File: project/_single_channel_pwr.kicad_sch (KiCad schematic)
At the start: 7 parts, among them Q301 AO3400A

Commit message: more layout
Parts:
- renumbered C301 to C13, C302 to C14, C303 to C15, D301 to D7, Q301 to Q2, R301 to R13, R302 to R14
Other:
- title: (none) -> LED Dimmer 6x6
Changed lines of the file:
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@@
 (kicad_sch (version 20211123) (generator eeschema)
   (paper "A4")
+  (title_block
+    (title "LED Dimmer 6x6")
+    (date "2025-01-13")
+    (rev "1.0")
+  )
   (junction (at 125.73 110.49) (diameter 0) (color 0 0 0 0)
   )
@@
   (symbol (lib_id "Transistor_FET:AO3400A") (at 142.24 110.49 0) (unit 1)
     (in_bom yes) (on_board yes)
-    (property "Reference" "Q301" (id 0) (at 144.78 114.3 0)
+    (property "Reference" "Q2" (id 0) (at 144.78 114.3 0)
       (effects (font (size 1.27 1.27)) (justify left))
     )
@@
   (symbol (lib_id "Device:C") (at 151.13 109.22 0) (unit 1)
     (in_bom yes) (on_board yes)
-    (property "Reference" "C303" (id 0) (at 152.4 106.68 0)
+    (property "Reference" "C15" (id 0) (at 152.4 106.68 0)
       (effects (font (size 1.27 1.27)) (justify left))
     )
@@
   (symbol (lib_id "Device:D_Schottky") (at 144.78 101.6 270) (unit 1)
     (in_bom yes) (on_board yes)
-    (property "Reference" "D301" (id 0) (at 138.43 99.06 90)
+    (property "Reference" "D7" (id 0) (at 138.43 99.06 90)
       (effects (font (size 1.27 1.27)) (justify left))
     )
@@
   (symbol (lib_id "Device:C") (at 125.73 114.3 0) (unit 1)
     (in_bom yes) (on_board yes)
-    (property "Reference" "C301" (id 0) (at 127 111.76 0)
+    (property "Reference" "C13" (id 0) (at 127 111.76 0)
       (effects (font (size 1.27 1.27)) (justify left))
     )
@@
   (symbol (lib_id "Device:C") (at 151.13 101.6 0) (unit 1)
     (in_bom yes) (on_board yes)
-    (property "Reference" "C302" (id 0) (at 152.4 99.06 0)
+    (property "Reference" "C14" (id 0) (at 152.4 99.06 0)
       (effects (font (size 1.27 1.27)) (justify left))
     )
@@
   (symbol (lib_id "Device:R") (at 134.62 114.3 180) (unit 1)
     (in_bom yes) (on_board yes)
-    (property "Reference" "R302" (id 0) (at 137.16 111.76 90)
+    (property "Reference" "R14" (id 0) (at 137.16 111.76 90)
       (effects (font (size 1.27 1.27)) (justify left))
     )
@@
   (symbol (lib_id "-pwr:GND") (at 144.78 118.11 0) (unit 1)
     (in_bom yes) (on_board yes)
-    (property "Reference" "#PWR0302" (id 0) (at 144.78 124.46 0)
+    (property "Reference" "#PWR033" (id 0) (at 144.78 124.46 0)
       (effects (font (size 1.27 1.27)) hide)
     )
@@
   (symbol (lib_id "power:+24V") (at 144.78 97.79 0) (unit 1)
     (in_bom yes) (on_board yes)
-    (property "Reference" "#PWR0301" (id 0) (at 144.78 101.6 0)
+    (property "Reference" "#PWR032" (id 0) (at 144.78 101.6 0)
       (effects (font (size 1.27 1.27)) hide)
     )
@@
   (symbol (lib_id "Device:R") (at 120.65 110.49 90) (unit 1)
     (in_bom yes) (on_board yes)
-    (property "Reference" "R301" (id 0) (at 123.19 107.95 90)
-      (effects (font (size 1.27 1.27)) (justify left))
-    )
+    (property "Reference" "R13" (id 0) (at 123.19 107.95 90)
+      (effects (font (size 1.27 1.27)) (justify left))
+    )

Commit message: prepared for production
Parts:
- C13, C14, C15: jlc-part-type (none) -> B; lcsc# C476766 -> C1710
- Q2: jlc-part-type (none) -> B
- R13: lcsc# C17630 -> C17513
- R14: lcsc# C17630 -> C149504
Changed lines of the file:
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@@
+      (effects (font (size 1.27 1.27)) hide)
+    )
+    (property "jlc-part-type" "B" (id 5) (at 142.24 110.49 0)
+      (effects (font (size 1.27 1.27)) hide)
+    )
+    (property "WE" "" (id 6) (at 142.24 110.49 0)
       (effects (font (size 1.27 1.27)) hide)
     )
@@
       (effects (font (size 1.27 1.27)) hide)
     )
-    (property "lcsc#" "C476766" (id 4) (at 151.13 109.22 0)
+    (property "lcsc#" "C1710" (id 4) (at 151.13 109.22 0)
+      (effects (font (size 1.27 1.27)) hide)
+    )
+    (property "jlc-part-type" "B" (id 5) (at 151.13 109.22 0)
+      (effects (font (size 1.27 1.27)) hide)
+    )
+    (property "WE" "" (id 6) (at 151.13 109.22 0)
       (effects (font (size 1.27 1.27)) hide)
     )
@@
       (effects (font (size 1.27 1.27)) hide)
     )
+    (property "WE" "" (id 6) (at 144.78 101.6 0)
+      (effects (font (size 1.27 1.27)) hide)
+    )
     (pin "1")
     (pin "2")
@@
       (effects (font (size 1.27 1.27)) hide)
     )
-    (property "lcsc#" "C476766" (id 4) (at 125.73 114.3 0)
+    (property "lcsc#" "C1710" (id 4) (at 125.73 114.3 0)
+      (effects (font (size 1.27 1.27)) hide)
+    )
+    (property "jlc-part-type" "B" (id 5) (at 125.73 114.3 0)
+      (effects (font (size 1.27 1.27)) hide)
+    )
+    (property "WE" "" (id 6) (at 125.73 114.3 0)
       (effects (font (size 1.27 1.27)) hide)
     )
@@
       (effects (font (size 1.27 1.27)) hide)
     )
-    (property "lcsc#" "C476766" (id 4) (at 151.13 101.6 0)
+    (property "lcsc#" "C1710" (id 4) (at 151.13 101.6 0)
+      (effects (font (size 1.27 1.27)) hide)
+    )
+    (property "jlc-part-type" "B" (id 5) (at 151.13 101.6 0)
+      (effects (font (size 1.27 1.27)) hide)
+    )
+    (property "WE" "" (id 6) (at 151.13 101.6 0)
       (effects (font (size 1.27 1.27)) hide)
     )
@@
       (effects (font (size 1.27 1.27)) hide)
     )
-    (property "lcsc#" "C17630" (id 5) (at 134.62 114.3 0)
+    (property "lcsc#" "C149504" (id 5) (at 134.62 114.3 0)
+      (effects (font (size 1.27 1.27)) hide)
+    )
+    (property "WE" "" (id 6) (at 134.62 114.3 0)
       (effects (font (size 1.27 1.27)) hide)
     )
@@
       (effects (font (size 1.27 1.27)) hide)
     )
-    (property "lcsc#" "C17630" (id 5) (at 120.65 110.49 0)
+    (property "lcsc#" "C17513" (id 5) (at 120.65 110.49 0)
       (effects (font (size 1.27 1.27)) hide)
     )
+    (property "WE" "" (id 6) (at 120.65 110.49 0)
+      (effects (font (size 1.27 1.27)) hide)
+    )

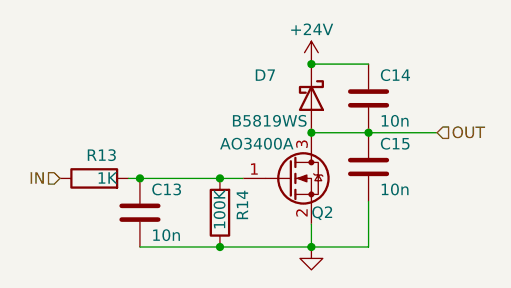
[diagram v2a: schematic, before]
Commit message: improvements after first prototype test
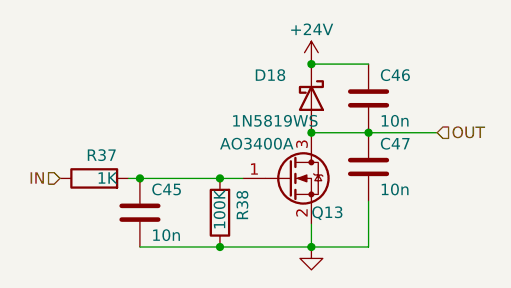
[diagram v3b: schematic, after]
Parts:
- D18: renamed from D7; value B5819WS -> 1N5819WS; jlc-part-type E -> B; lcsc# C169530 -> C191023
- renumbered C13 to C45, C14 to C46, C15 to C47, Q2 to Q13, R13 to R37, R14 to R38
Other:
- title: LED Dimmer 6x6 -> LED_Dimmer_6x6
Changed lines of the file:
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@@
   (paper "A4")
   (title_block
-    (title "LED Dimmer 6x6")
+    (title "LED_Dimmer_6x6")
     (date "2025-01-13")
-    (rev "1.0")
+    (rev "1.1")
   )
   (junction (at 125.73 110.49) (diameter 0) (color 0 0 0 0)
@@
   (symbol (lib_id "Transistor_FET:AO3400A") (at 142.24 110.49 0) (unit 1)
     (in_bom yes) (on_board yes)
-    (property "Reference" "Q2" (id 0) (at 144.78 114.3 0)
+    (property "Reference" "Q13" (id 0) (at 144.78 114.3 0)
       (effects (font (size 1.27 1.27)) (justify left))
     )
@@
   (symbol (lib_id "Device:C") (at 151.13 109.22 0) (unit 1)
     (in_bom yes) (on_board yes)
-    (property "Reference" "C15" (id 0) (at 152.4 106.68 0)
+    (property "Reference" "C47" (id 0) (at 152.4 106.68 0)
       (effects (font (size 1.27 1.27)) (justify left))
     )
@@
   (symbol (lib_id "Device:D_Schottky") (at 144.78 101.6 270) (unit 1)
     (in_bom yes) (on_board yes)
-    (property "Reference" "D7" (id 0) (at 138.43 99.06 90)
-      (effects (font (size 1.27 1.27)) (justify left))
-    )
-    (property "Value" "B5819WS" (id 1) (at 135.89 104.14 90)
+    (property "Reference" "D18" (id 0) (at 138.43 99.06 90)
+      (effects (font (size 1.27 1.27)) (justify left))
+    )
+    (property "Value" "1N5819WS" (id 1) (at 135.89 104.14 90)
       (effects (font (size 1.27 1.27)) (justify left))
     )
@@
       (effects (font (size 1.27 1.27)) hide)
     )
-    (property "Datasheet" "https://www.lcsc.com/datasheet/lcsc_datasheet_1811011616_Shandong-Jingdao-Microelectronics-B5819WS_C169530.pdf" (id 3) (at 144.78 101.6 0)
-      (effects (font (size 1.27 1.27)) hide)
-    )
-    (property "lcsc#" "C169530" (id 4) (at 144.78 101.6 0)
-      (effects (font (size 1.27 1.27)) hide)
-    )
-    (property "jlc-part-type" "E" (id 5) (at 144.78 101.6 0)
+    (property "Datasheet" "" (id 3) (at 144.78 101.6 0)
+      (effects (font (size 1.27 1.27)) hide)
+    )
+    (property "lcsc#" "C191023" (id 4) (at 144.78 101.6 0)
+      (effects (font (size 1.27 1.27)) hide)
+    )
+    (property "jlc-part-type" "B" (id 5) (at 144.78 101.6 0)
       (effects (font (size 1.27 1.27)) hide)
     )
@@
   (symbol (lib_id "Device:C") (at 125.73 114.3 0) (unit 1)
     (in_bom yes) (on_board yes)
-    (property "Reference" "C13" (id 0) (at 127 111.76 0)
+    (property "Reference" "C45" (id 0) (at 127 111.76 0)
       (effects (font (size 1.27 1.27)) (justify left))
     )
@@
   (symbol (lib_id "Device:C") (at 151.13 101.6 0) (unit 1)
     (in_bom yes) (on_board yes)
-    (property "Reference" "C14" (id 0) (at 152.4 99.06 0)
+    (property "Reference" "C46" (id 0) (at 152.4 99.06 0)
       (effects (font (size 1.27 1.27)) (justify left))
     )
@@
   (symbol (lib_id "Device:R") (at 134.62 114.3 180) (unit 1)
     (in_bom yes) (on_board yes)
-    (property "Reference" "R14" (id 0) (at 137.16 111.76 90)
+    (property "Reference" "R38" (id 0) (at 137.16 111.76 90)
       (effects (font (size 1.27 1.27)) (justify left))
     )
@@
   (symbol (lib_id "-pwr:GND") (at 144.78 118.11 0) (unit 1)
     (in_bom yes) (on_board yes)
-    (property "Reference" "#PWR033" (id 0) (at 144.78 124.46 0)
+    (property "Reference" "#PWR055" (id 0) (at 144.78 124.46 0)
       (effects (font (size 1.27 1.27)) hide)
     )
@@
   (symbol (lib_id "power:+24V") (at 144.78 97.79 0) (unit 1)
     (in_bom yes) (on_board yes)
-    (property "Reference" "#PWR032" (id 0) (at 144.78 101.6 0)
+    (property "Reference" "#PWR054" (id 0) (at 144.78 101.6 0)
       (effects (font (size 1.27 1.27)) hide)
     )
@@
   (symbol (lib_id "Device:R") (at 120.65 110.49 90) (unit 1)
     (in_bom yes) (on_board yes)
-    (property "Reference" "R13" (id 0) (at 123.19 107.95 90)
-      (effects (font (size 1.27 1.27)) (justify left))
-    )
+    (property "Reference" "R37" (id 0) (at 123.19 107.95 90)
+      (effects (font (size 1.27 1.27)) (justify left))
+    )
